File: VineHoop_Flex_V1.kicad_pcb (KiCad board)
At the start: 2 copper layers, 63.1 x 15.8 mm, 31 parts, among them J1 Conn_01x06_Female, J2 Conn_01x06_Female, J3 Conn_01x04_Female, U1 MIC5205-3.3YM5, U2 SHT31-DIS-B, U3 BNO055, U4 ATMEGA328P-MUR, Y1 32.768kHz, Y2 16MHz

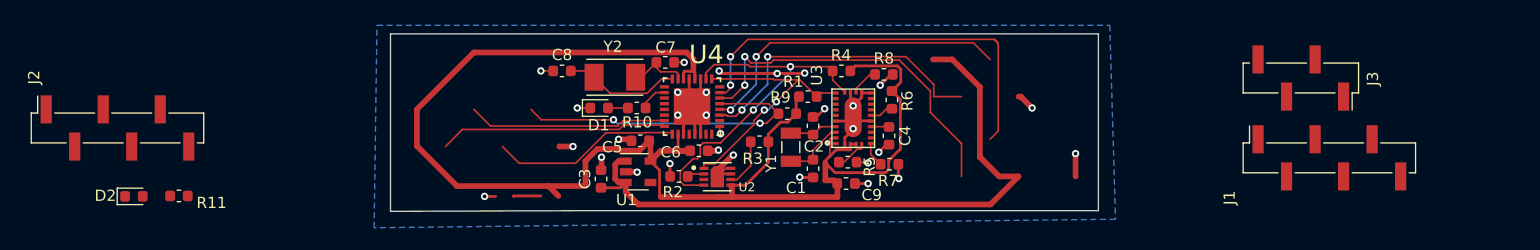
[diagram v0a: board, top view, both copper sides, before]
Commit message: First rev spread out flexpcb
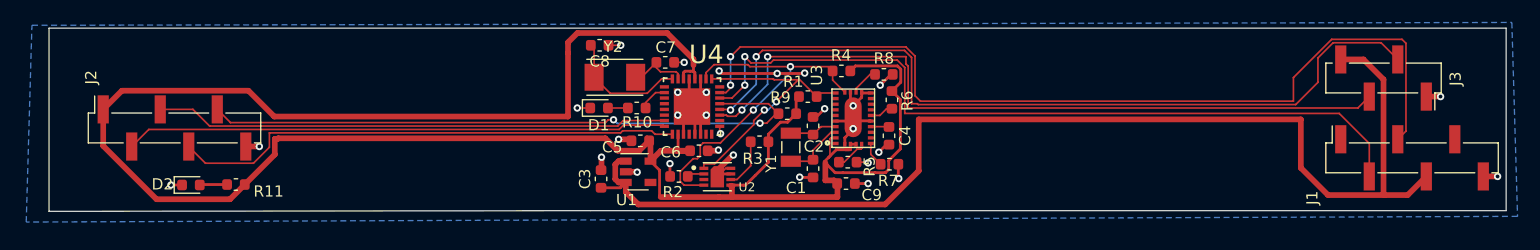
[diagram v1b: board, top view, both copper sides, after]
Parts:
- moved J1 7.37 mm to (213.4, 67.4)
- moved J3 7.37 mm to (210.8, 60.3)
- moved D2 5.18 mm to (104.6, 69.8)
- moved R11 5.18 mm to (108.6, 69.8)
- moved J2 5.08 mm to (103.1, 64.8)
- moved C8 4.06 mm to (141.0, 57.4), turned to 180 degrees
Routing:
- net +3V3: track 132.5 -> 195.7 mm
- net VDD: track 58.7 -> 105.2 mm
- net SCL: track 28.6 -> 72.6 mm
- net TX: track 37.9 -> 81.0 mm
- net SDA: track 27.3 -> 66.4 mm
- net RX: track 32.0 -> 69.6 mm
- net SCK: track 16.9 -> 45.8 mm
- net RESET: track 28.5 -> 56.7 mm
- net MISO: track 20.3 -> 48.3 mm
- net MOSI: track 17.8 -> 45.7 mm
- net Net-(C8-Pad2): track 10.4 -> 11.9 mm
- net GND: track 60.4 -> 59.2 mm
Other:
- board size 63.1 x 15.8 mm -> 129.8 x 16.3 mm

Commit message: So much stuff
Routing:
- net +3V3: track 195.7 -> 194.7 mm
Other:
- board size 129.8 x 16.3 mm -> 127 x 16.3 mm

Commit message: Lots of changes incl. "final" gerbers for rigid order
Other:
- net class Default removed
- net class Power removed
